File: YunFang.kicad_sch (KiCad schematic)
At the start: 0 parts

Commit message: 增加预驱/三相桥电路
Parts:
- added U3: ~, Package_SO:SSOP-14_5.3x6.2mm_P0.65mm, symbol User_Driver:LMV324IDT

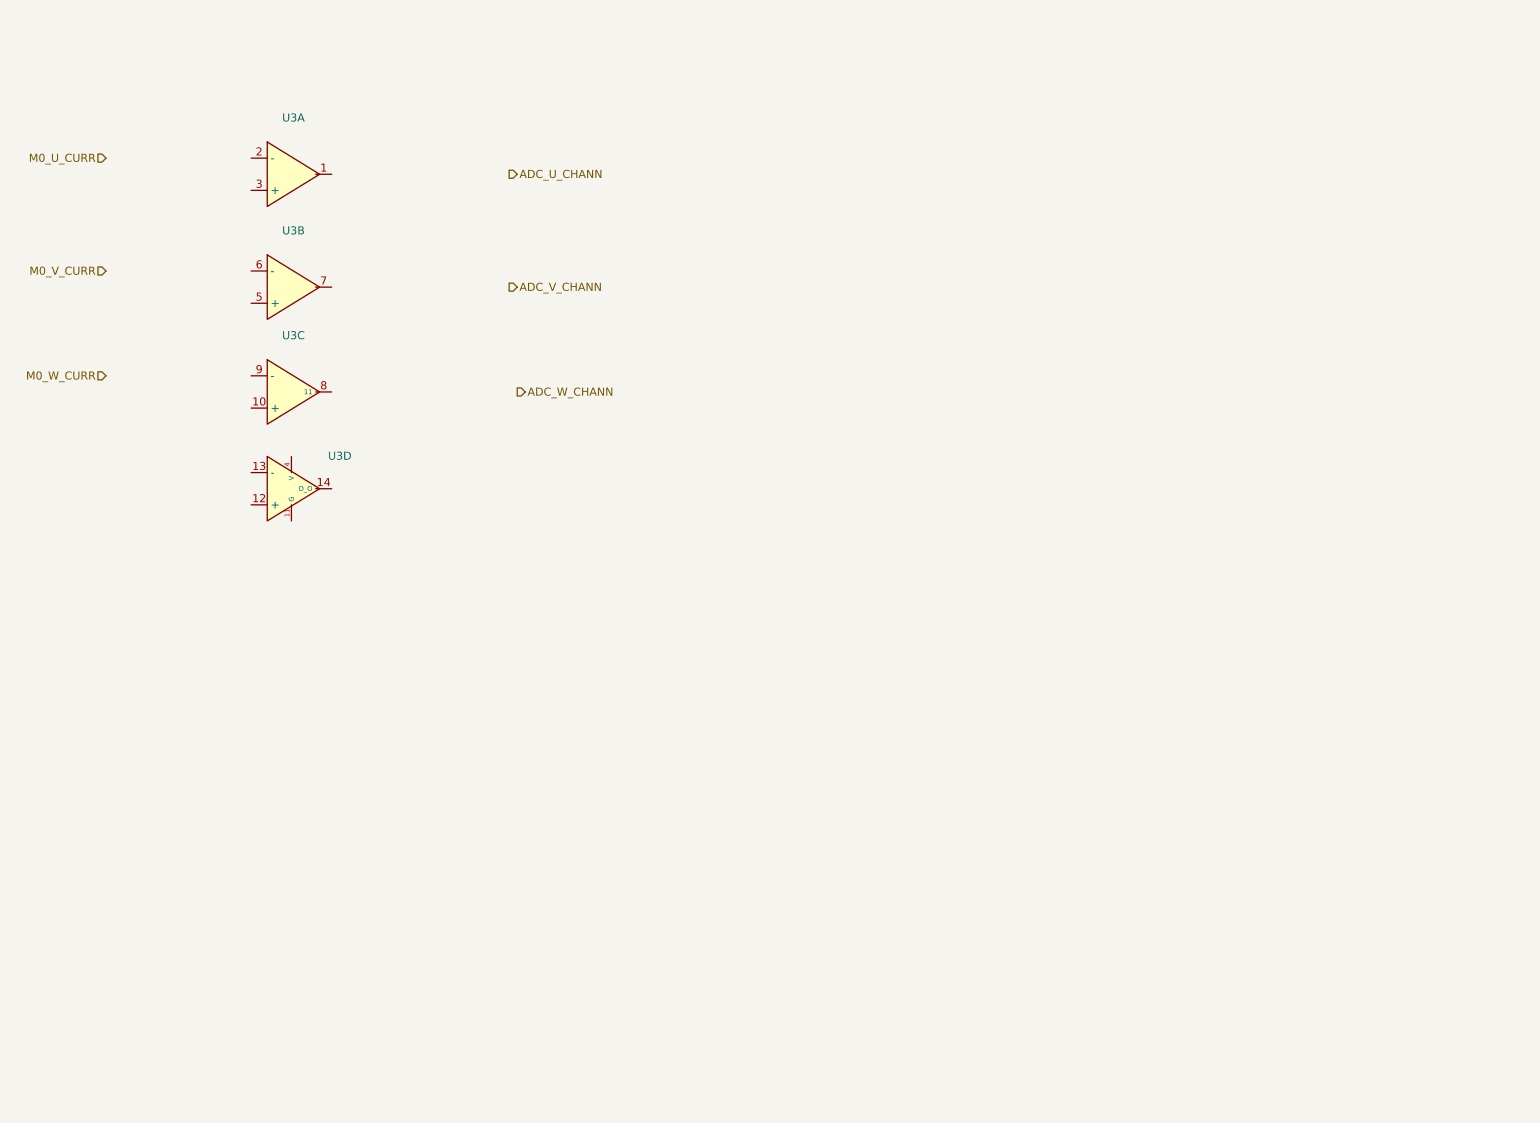
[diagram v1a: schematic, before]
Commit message: 优化5V电源/预驱电路/三相桥/运放
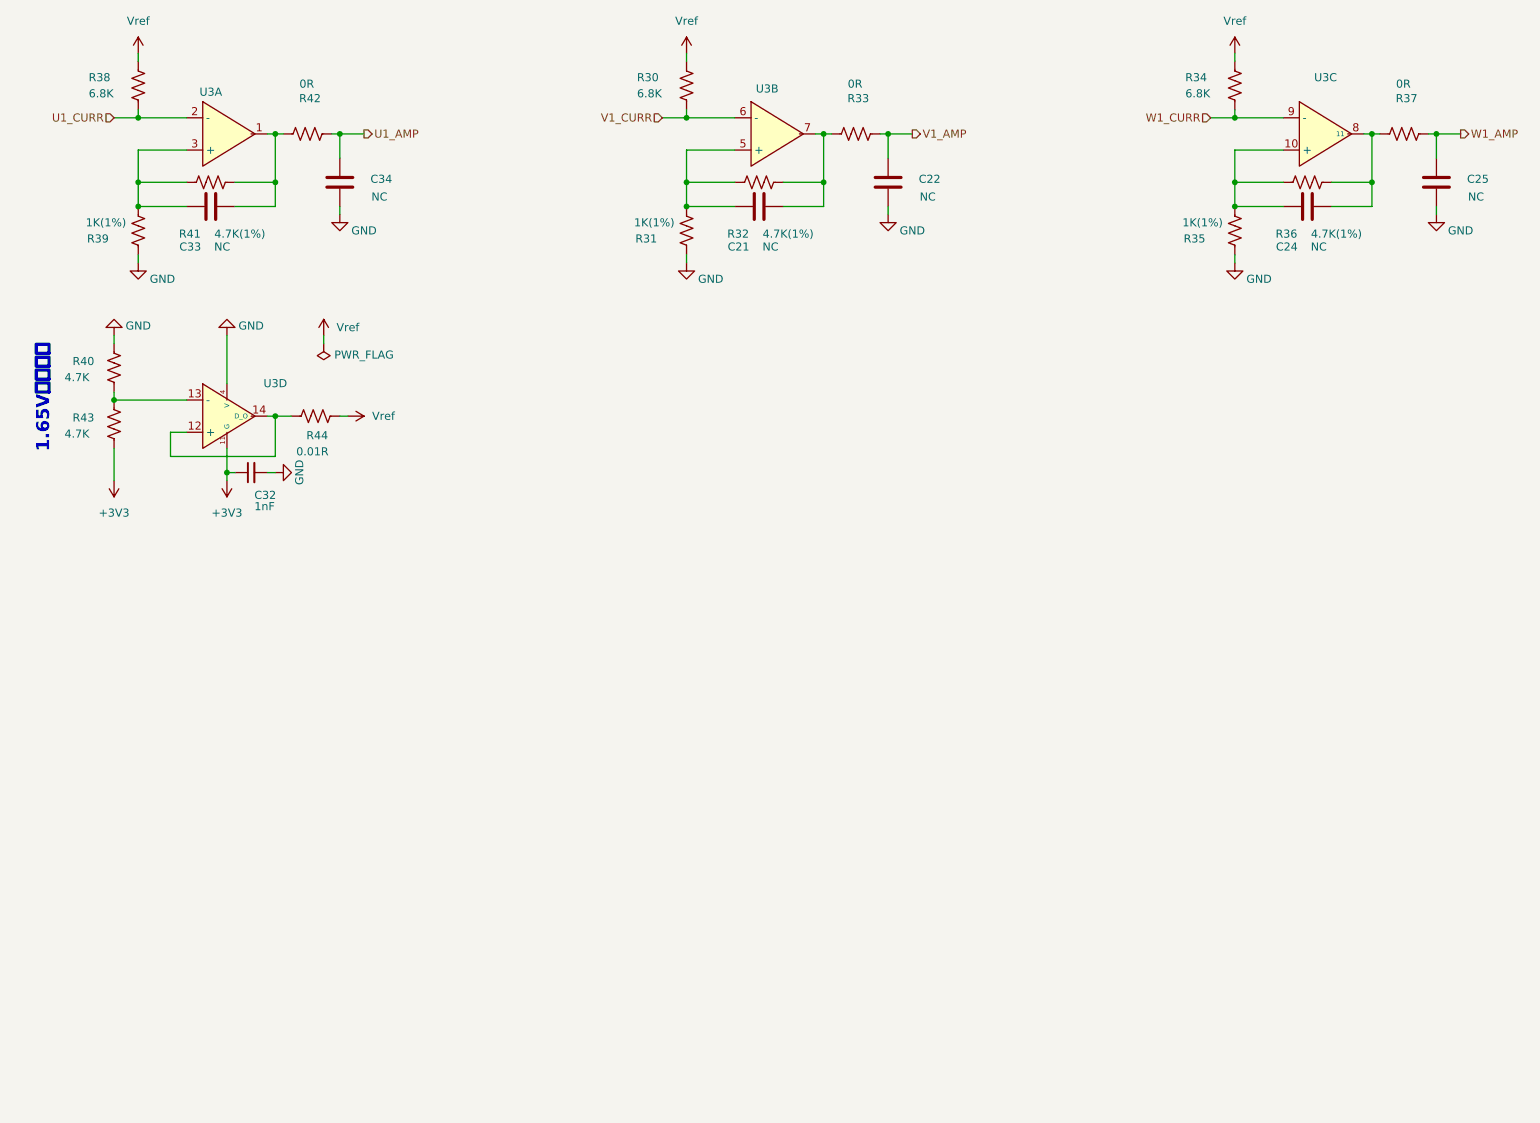
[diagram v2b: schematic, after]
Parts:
- added C21, C22, C24, C25, C33, C34: NC, Capacitor_SMD:C_0603_1608Metric, symbol Device:C
- added C32: 1nF, Capacitor_SMD:C_0603_1608Metric, symbol Device:C_Small
- added R30, R34, R38: 6.8K, Resistor_SMD:R_0603_1608Metric, symbol Device:R_US
- added R31, R35, R39: 1K(1%), Resistor_SMD:R_0603_1608Metric, symbol Device:R_US
- added R32, R36, R41: 4.7K(1%), Resistor_SMD:R_0603_1608Metric, symbol Device:R_US
- added R33, R37, R42: 0R, Resistor_SMD:R_0603_1608Metric, symbol Device:R_US
- added R40, R43: 4.7K, Resistor_SMD:R_0603_1608Metric, symbol Device:R_US
- added R44: 0.01R, Resistor_SMD:R_0603_1608Metric_Pad0.98x0.95mm_HandSolder, symbol Device:R_US
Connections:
- net at U3.1: now also C33.2, R41.2, R42.1
- net U1_CURR: now reaches U3.2 (-)
- net U1_CURR: now also R38.2
- net at U3.3 (+): now also C33.1, R39.2, R41.1
- net at U3.10 (+): now also C24.1, R35.2, R36.1
- net at U3.8 (11): now also C24.2, R36.2, R37.1
- net W1_CURR: now reaches U3.9 (-)
- net W1_CURR: now also R34.2
- net +3V3: now reaches U3.11 (G)
- net +3V3: now also C32.1, R43.1
- net at U3.12 (+): now also U3.14 (D_O), R44.2
- net at U3.13 (-): now also R40.1, R43.2
- net GND: now reaches U3.4 (V)
- net GND: now also C22.1, C25.1, C32.2, C34.1, R31.1, R35.1, R39.1, R40.2
- net at U3.5 (+): now also C21.1, R31.2, R32.1
- net V1_CURR: now reaches U3.6 (-)
- net V1_CURR: now also R30.2
- net at U3.7: now also C21.2, R32.2, R33.1
- new net U1_AMP: C34.2, R42.2
- new net V1_AMP: C22.2, R33.2
- new net Vref: R30.1, R34.1, R38.1, R44.1
- new net W1_AMP: C25.2, R37.2
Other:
- note added: "1.65V基准电压"
- moved on the sheet: U3A, U3C, U3D

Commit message: 优化原理图
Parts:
- renumbered C33 to C34, C32 to C35, C34 to C36, C21 to C37, C22 to C38, C24 to C39, C25 to C40, R40 to R24, R43 to R25, R38 to R26, R39 to R27, R41 to R28, R42 to R29, R44 to R30, R30 to R31, R31 to R32, R32 to R33, R33 to R34, R34 to R35, R35 to R36, R36 to R37, R37 to R38, U3 to U5

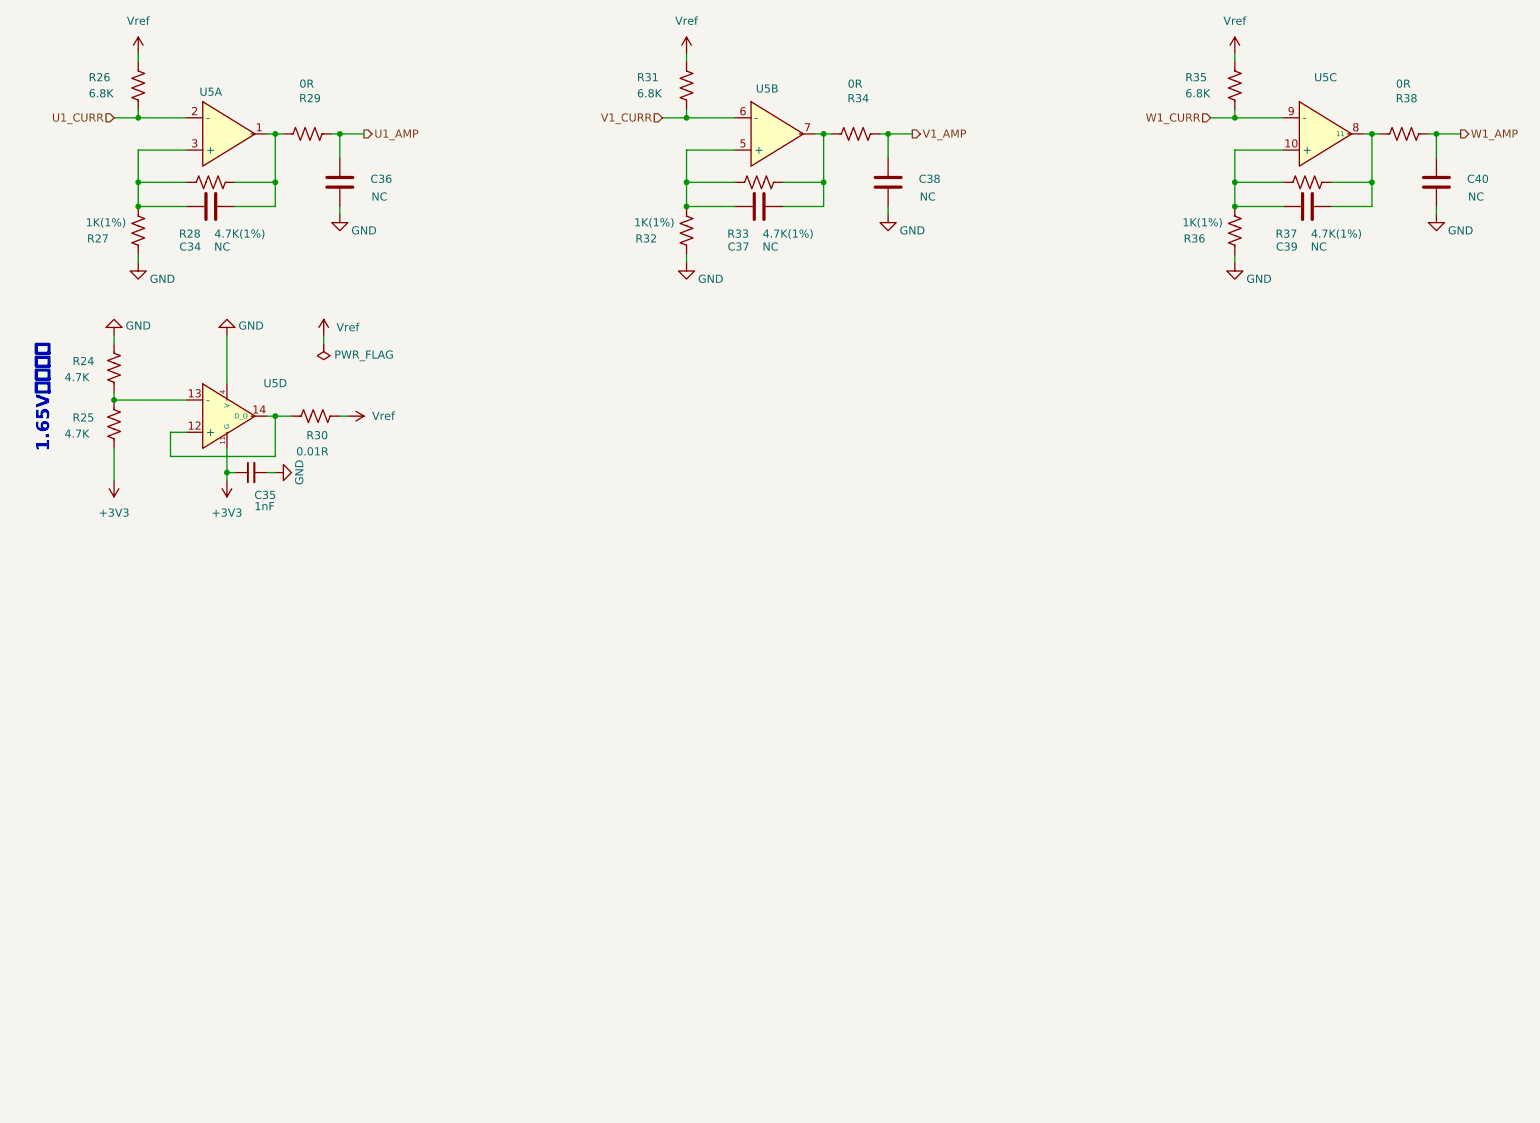
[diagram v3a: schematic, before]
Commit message: 原理图增加motor2部分
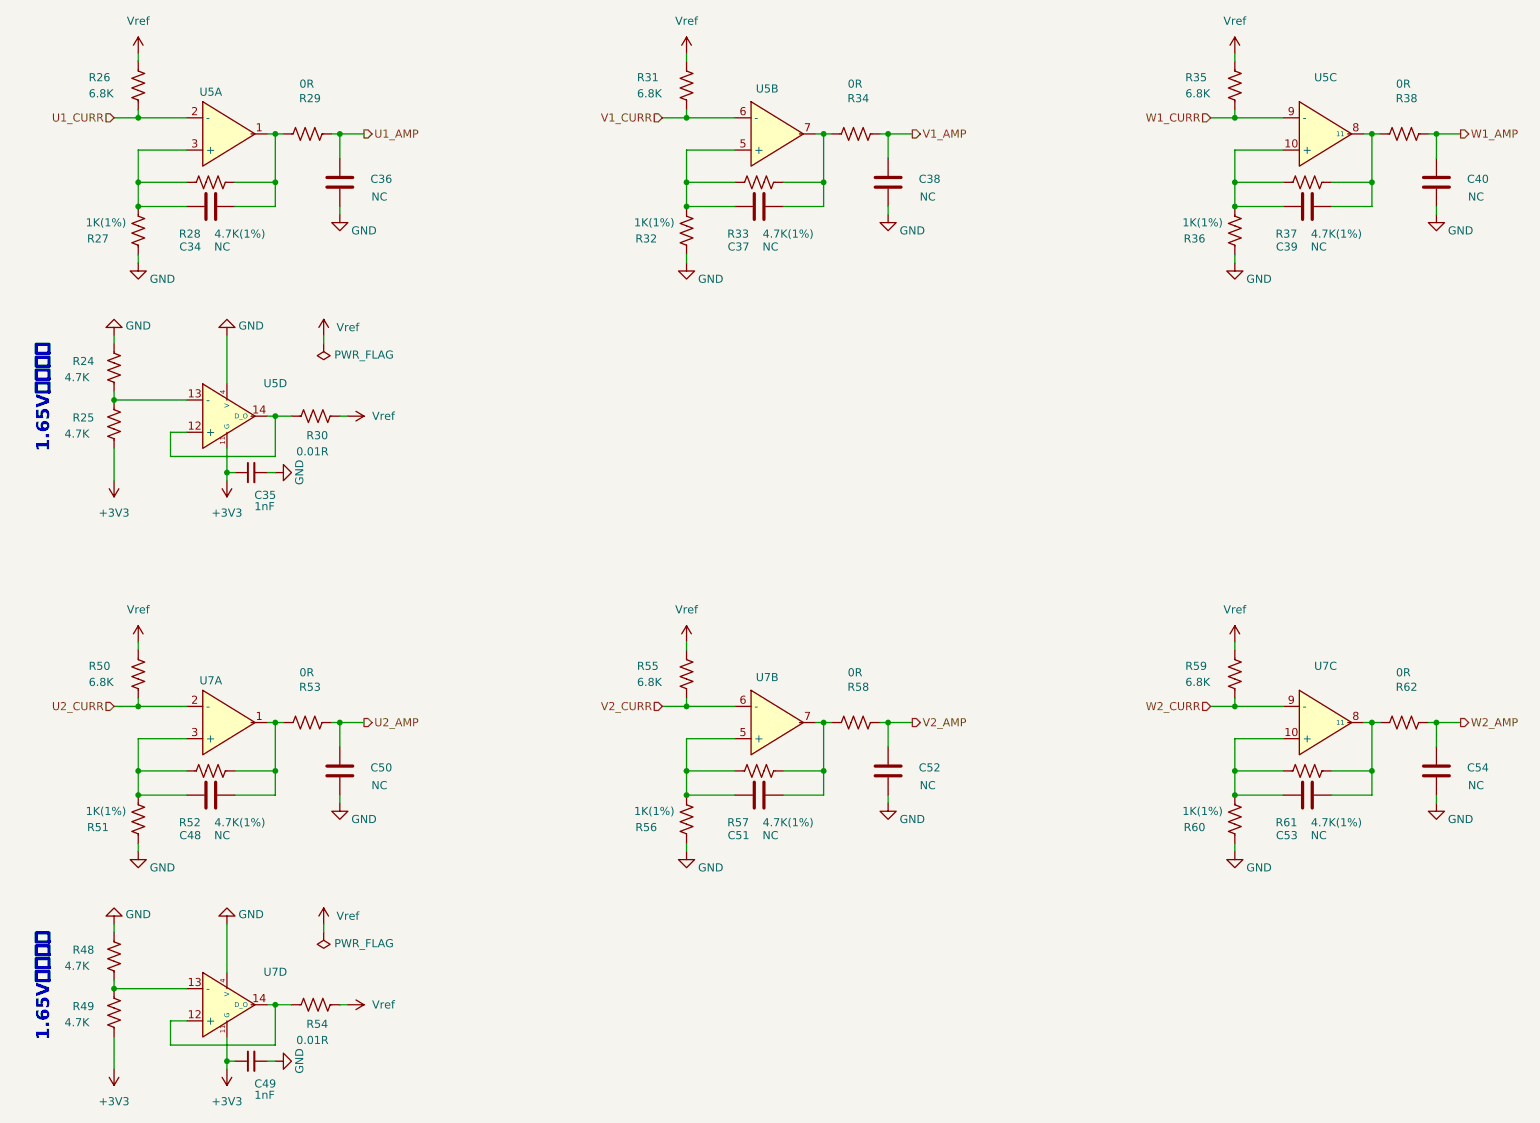
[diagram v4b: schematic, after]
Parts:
- added C48, C50, C51, C52, C53, C54: NC, Capacitor_SMD:C_0603_1608Metric, symbol Device:C
- added C49: 1nF, Capacitor_SMD:C_0603_1608Metric, symbol Device:C_Small
- added R48, R49: 4.7K, Resistor_SMD:R_0603_1608Metric, symbol Device:R_US
- added R50, R55, R59: 6.8K, Resistor_SMD:R_0603_1608Metric, symbol Device:R_US
- added R51, R56, R60: 1K(1%), Resistor_SMD:R_0603_1608Metric, symbol Device:R_US
- added R52, R57, R61: 4.7K(1%), Resistor_SMD:R_0603_1608Metric, symbol Device:R_US
- added R53, R58, R62: 0R, Resistor_SMD:R_0603_1608Metric, symbol Device:R_US
- added R54: 0.01R, Resistor_SMD:R_0603_1608Metric_Pad0.98x0.95mm_HandSolder, symbol Device:R_US
- added U7: ~, Package_SO:SSOP-14_5.3x6.2mm_P0.65mm, symbol User_Driver:LMV324IDT
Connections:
- net +3V3: now also C49.1, R49.1, U7.11 (G)
- net GND: now also C49.2, C50.1, C52.1, C54.1, R48.2, R51.1, R56.1, R60.1, U7.4 (V)
- net Vref: now also R50.1, R54.1, R55.1, R59.1
- new net: C53.1, R60.2, R61.1, U7.10 (+)
- new net: C53.2, R61.2, R62.1, U7.8 (11)
- new net: C51.1, R56.2, R57.1, U7.5 (+)
- new net: C51.2, R57.2, R58.1, U7.7
- new net: C48.2, R52.2, R53.1, U7.1
- new net: C48.1, R51.2, R52.1, U7.3 (+)
- new net: R54.2, U7.12 (+), U7.14 (D_O)
- new net: R48.1, R49.2, U7.13 (-)
- new net U2_AMP: C50.2, R53.2
- new net U2_CURR: R50.2, U7.2 (-)
- new net V2_AMP: C52.2, R58.2
- new net V2_CURR: R55.2, U7.6 (-)
- new net W2_AMP: C54.2, R62.2
- new net W2_CURR: R59.2, U7.9 (-)
